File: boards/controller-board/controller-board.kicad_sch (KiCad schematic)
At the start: 163 parts, among them J1 Conn_01x02, J2 Conn_01x02, J3 Conn_01x02, J4 Conn_01x02, J5 Conn_01x03, J6 Conn_01x02, Q1 Goford_G11S_20V_11A, Q2 PMV45EN, SW1 EG1271, U1 CAT4201, U10 CAT4201, U11 CAT4201, U12 CAT4201, U13 CAT4201, U14 CAT4201, U15 CAT4201, U17 CAT4201, U18 CAT4201, U25 RPi_Pico, U3 LTC3624, U4 CAT4201, U5 CAT4201, U6 CAT4201, U7 MCP4728, U8 ADS1015IRUGR, U9 ADS1015IRUGR

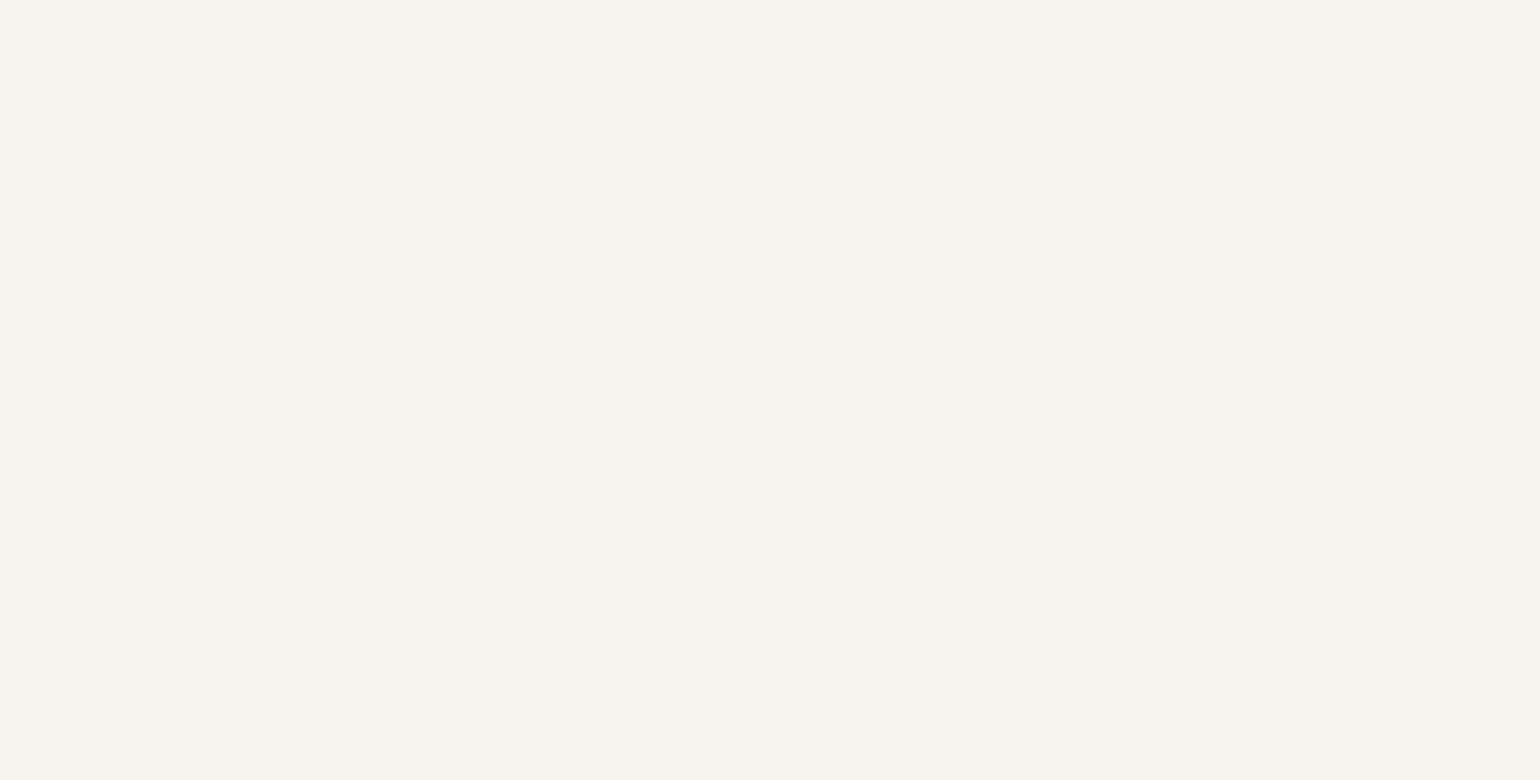
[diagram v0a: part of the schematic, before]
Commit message: added new design for LED driver portion of circuit with A6214
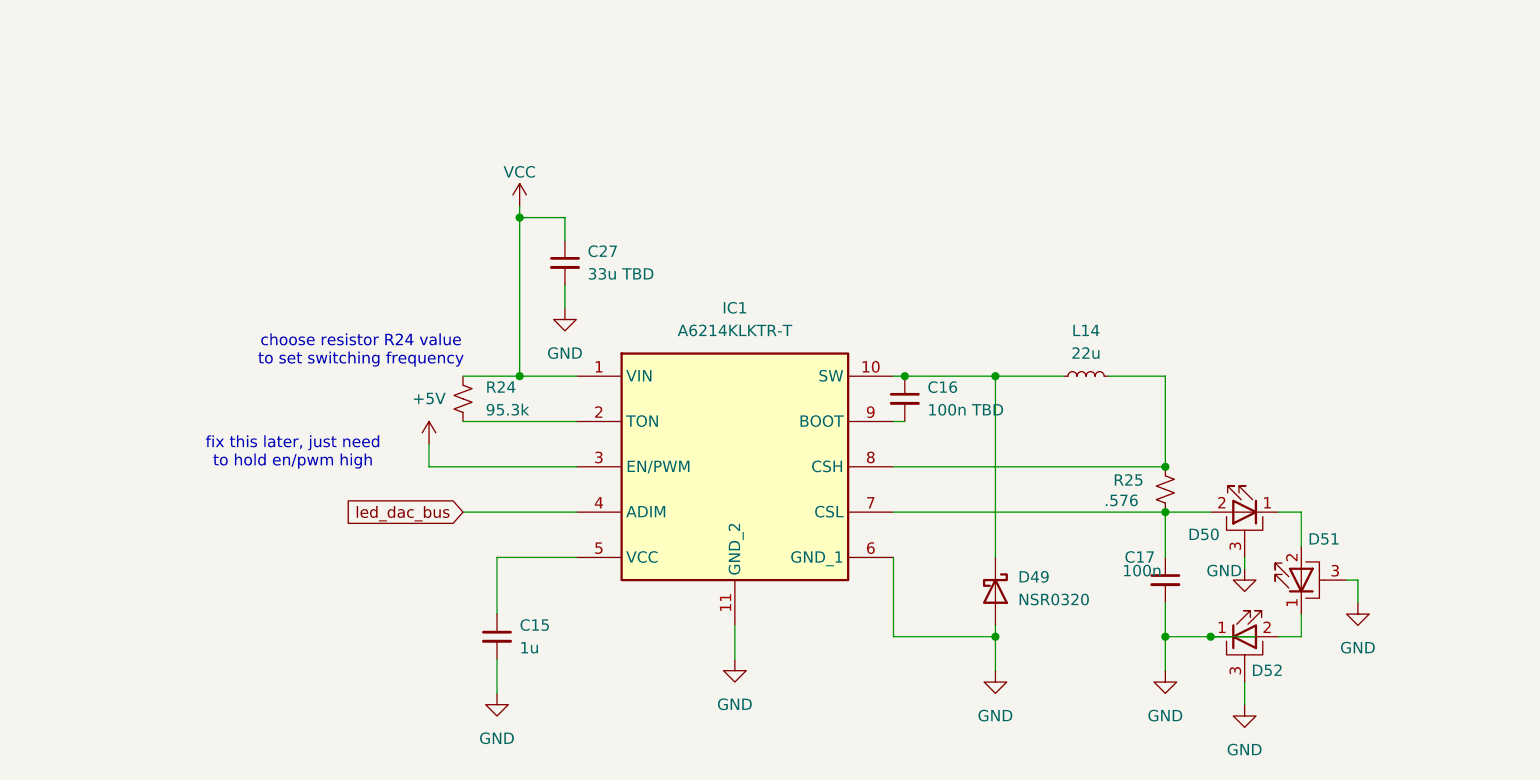
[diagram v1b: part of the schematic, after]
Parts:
- added C15: 1u, symbol Device:C_Small
- added C16: 100n TBD, symbol Device:C_Small
- added C17: 100n, symbol Device:C_Small
- added C27: 33u TBD, symbol Device:C_Small
- added D49: NSR0320, symbol Device:D_Schottky
- added D50, D51, D52: XPEBBL-L1-0000-00201, oresat-diodes:Cree-LED, symbol Device:LED_Pad
- added IC1: A6214KLKTR-T, oresat-ics:SOP100P600X165-11N, symbol oresat-ics:A6214KLKTR-T
- added L14: 22u, symbol Device:L_Small
- added R24: 95.3k, symbol Device:R_Small_US
- added R25: .576, symbol Device:R_Small_US
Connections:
- net +5V: now also IC1.3 (EN/PWM)
- net GND: now also C15.2, C17.2, C27.2, D49.2 (A), D50.3 (PAD), D51.3 (PAD), D52.1 (K), D52.3 (PAD), IC1.11 (GND_2), IC1.6 (GND_1)
- net VCC: now also C27.1, IC1.1 (VIN), R24.1
- new net: D51.1 (K), D52.2 (A)
- new net: C16.1, D49.1 (K), IC1.10 (SW), L14.1
- new net: IC1.2 (TON), R24.2
- new net: C15.1, IC1.5 (VCC)
- new net: C17.1, D50.2 (A), IC1.7 (CSL), R25.2
- new net: IC1.8 (CSH), L14.2, R25.1
- new net: C16.2, IC1.9 (BOOT)
- new net: D50.1 (K), D51.2 (A)
- new net led_dac_bus: IC1.4 (ADIM)
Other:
- note added: "choose resistor R24 value to set switching frequency"
- note added: "fix this later, just need to hold en/pwm high"

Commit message: added project for test board for new LED driver
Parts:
- removed C25, C34: 4.7u, Capacitor_SMD:C_0603_1608Metric, symbol Device:C_Small
- removed C26, C36: 22u, Capacitor_SMD:C_1210_3225Metric, symbol Device:C_Small
- removed D34, D7: NSR0320, Diode_SMD:D_SOD-323, symbol Device:D_Schottky
- removed D38, D39, D41: XPEBBL-L1-0000-00201, oresat-diodes:Cree-LED, symbol Device:LED_Pad
- removed D5, D6, D8: XPEBRD-L1-0000-00501, oresat-diodes:Cree-LED, symbol Device:LED_Pad
- removed L6, L9: 56u, Inductor_SMD:L_Wuerth_HCI-5040, symbol Device:L_Small
- removed R14, R18: 10k, Resistor_SMD:R_0603_1608Metric, symbol Device:R_Small_US
- removed U10, U13: CAT4201, Package_TO_SOT_SMD:TSOT-23-5, symbol oresat-ics:CAT4201
- added C32: 33u TBD, symbol Device:C_Small
- added C33: 1u, symbol Device:C_Small
- added C38: 100n TBD, symbol Device:C_Small
- added C39: 100n, symbol Device:C_Small
- added D53: NSR0320, symbol Device:D_Schottky
- added D54, D55, D56: XPEBBL-L1-0000-00201, oresat-diodes:Cree-LED, symbol Device:LED_Pad
- added IC2: A6214KLKTR-T, oresat-ics:SOP100P600X165-11N, symbol oresat-ics:A6214KLKTR-T
- added L15: 22u, symbol Device:L_Small
- added R26: 95.3k, symbol Device:R_Small_US
- added R27: .576, symbol Device:R_Small_US
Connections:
- net +5V: now also IC2.3 (EN/PWM)
- net GND: now also C32.2, C33.2, C39.2, D53.2 (A), D54.3 (PAD), D55.1 (K), D55.3 (PAD), D56.3 (PAD), IC2.11 (GND_2), IC2.6 (GND_1)
- net RED_LIM: no longer U1.1 (CTRL)
- net VCC: now also C32.1, IC2.1 (VIN), R26.1
- net led_dac_bus: now also IC2.4 (ADIM); no longer IC1.4 (ADIM)
- new net: IC2.8 (CSH), L15.2, R27.1
- new net: C39.1, D54.2 (A), IC2.7 (CSL), R27.2
- new net: D54.1 (K), D56.2 (A)
- new net: IC2.2 (TON), R26.2
- new net: C38.1, D53.1 (K), IC2.10 (SW), L15.1
- new net: C38.2, IC2.9 (BOOT)
- new net: D55.2 (A), D56.1 (K)
- new net: C33.1, IC2.5 (VCC)
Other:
- moved on the sheet: C1, C11, C12, C13, C16, C17, C2, C27, C28, C29, C3, C30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

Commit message: edited schematic to include new LED driver on new page
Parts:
- removed C1: 22u, oresat-diodes:Cree-LED, symbol Device:C_Small
- removed C11: 4.7u, Capacitor_SMD:C_0603_1608Metric, symbol Device:C_Small
- removed C32: 33u TBD, symbol Device:C_Small
- removed C33: 1u, symbol Device:C_Small
- removed C38: 100n TBD, symbol Device:C_Small
- removed C39: 100n, symbol Device:C_Small
- removed D1: NSR0320, Diode_SMD:D_SOD-323, symbol Device:D_Schottky
- removed D25, D26, D27: XPEBRD-L1-0000-00501, oresat-diodes:Cree-LED, symbol Device:LED_Pad
- removed D53: NSR0320, symbol Device:D_Schottky
- removed D54, D55, D56: XPEBBL-L1-0000-00201, oresat-diodes:Cree-LED, symbol Device:LED_Pad
- removed IC2: A6214KLKTR-T, oresat-ics:SOP100P600X165-11N, symbol oresat-ics:A6214KLKTR-T
- removed L1: 56u, Inductor_SMD:L_Wuerth_HCI-5040, symbol Device:L_Small
- removed L15: 22u, symbol Device:L_Small
- removed R2: 10k, Resistor_SMD:R_0603_1608Metric, symbol Device:R_Small_US
- removed R26: 95.3k, symbol Device:R_Small_US
- removed R27: .576, symbol Device:R_Small_US
- removed U1: CAT4201, Package_TO_SOT_SMD:TSOT-23-5, symbol oresat-ics:CAT4201
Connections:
- no-connect marks 26 -> 27
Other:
- added sheet Untitled Sheet (untitled.kicad_sch)
- note removed: "fix this later, just need to hold en/pwm high"

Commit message: cleaned up controller schematic
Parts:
- removed C15: 1u, symbol Device:C_Small
- removed C16: 100n TBD, symbol Device:C_Small
- removed C17: 100n, symbol Device:C_Small
- removed C27: 33u TBD, symbol Device:C_Small
- removed D49: NSR0320, symbol Device:D_Schottky
- removed D50, D51, D52: XPEBBL-L1-0000-00201, oresat-diodes:Cree-LED, symbol Device:LED_Pad
- removed IC1: A6214KLKTR-T, oresat-ics:SOP100P600X165-11N, symbol oresat-ics:A6214KLKTR-T
- removed L14: 22u, symbol Device:L_Small
- removed R24: 95.3k, symbol Device:R_Small_US
- removed R25: .576, symbol Device:R_Small_US
- renumbered C5 to C1, C9 to C10, C43 to C15, C44 to C16, C51 to C17, C20 to C18, C6 to C2, C2 to C20, C3 to C21, C28 to C22, C29 to C23, C12 to C24, C13 to C25, C30 to C26, C31 to C27, C35 to C28, C4 to C29, C10 to C3, C14 to C30, C45 to C31, C46 to C32, C37 to C33, C18 to C34, C40 to C35, C47 to C36, C48 to C37, C23 to C4, C21 to C5, C24 to C6, C22 to C7, C7 to C8, C8 to C9, D12 to D10, D9 to D11, D10 to D12, D30 to D13, D31 to D14, D28 to D15, D29 to D16, D14 to D17, D13 to D18, D33 to D19, D32 to D20, D35 to D21, D4 to D22, D17 to D23, D42 to D25, D36 to D26, D37 to D27, D20 to D28, D21 to D29, D18 to D30, D19 to D31, D45 to D32, D46 to D33, D43 to D34, D44 to D35, D40 to D36, D23 to D37, D22 to D38, D48 to D39, D47 to D40, D2 to D5, D3 to D6, D15 to D7, D16 to D8, D11 to D9, L5 to L1, L12 to L10, L13 to L11, L2 to L3, L3 to L4, L7 to L5, L8 to L6, L10 to L7, L4 to L8, L11 to L9, Q2 to Q1, Q1 to Q2, R15 to R10, R23 to R12, R10 to R13, R3 to R14, R4 to R15, R19 to R18, R5 to R19, R6 to R2, R7 to R3, R8 to R4, R9 to R5, R12 to R7, R13 to R8, R11 to R9, TP7 to TP1, TP6 to TP2, TP9 to TP3, TP1 to TP4, TP2 to TP5, TP3 to TP6, TP4 to TP7, TP5 to TP8, TP8 to TP9, U3 to U1, U14 to U10, U6 to U11, U15 to U12, U17 to U13, U18 to U14, U8 to U2, U9 to U3, U25 to U4, U7 to U5, U4 to U6, U5 to U7, U11 to U8, U12 to U9
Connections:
- no-connect marks 27 -> 26
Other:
- note removed: "choose resistor R24 value to set switching frequency"
- moved on the sheet: C1, C10, C15, C16, C17, C18, C19, C2, C20, C21, C22, C23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

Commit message: redesigned pcb
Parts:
- removed C20, C21, C22, C23, C28, C29, C30, C31, C32: 4.7u, Capacitor_SMD:C_0603_1608Metric, symbol Device:C_Small
- removed C24, C25, C26, C27, C33, C34, C35, C36, C37: 22u, Capacitor_SMD:C_1210_3225Metric, symbol Device:C_Small
- removed D10, D11, D12, D17, D18, D9: XPEBGR-L1-0000-00D01, oresat-diodes:Cree-LED, symbol Device:LED_Pad
- removed D13, D14, D15, D16, D19, D20, D26, D27, D36: XPEBBL-L1-0000-00201, oresat-diodes:Cree-LED, symbol Device:LED_Pad
- removed D21, D22, D23, D24, D25, D5, D6, D7, D8: NSR0320, Diode_SMD:D_SOD-323, symbol Device:D_Schottky
- removed D28, D29, D30, D31: ELUA3535OGB-P6070U23240500-VD1M, oresat-diodes:Cree-LED, symbol Device:LED_Pad
- removed D32, D33, D34, D35: ELUC3535NUB-P7085Q15070100-S22Q, oresat-diodes:Cree-LED, symbol Device:LED_Pad
- removed D37, D38, D39, D40: NP, oresat-diodes:Cree-LED, symbol Device:LED_Pad
- removed L10, L11, L3, L4, L5, L6, L7, L8, L9: 56u, Inductor_SMD:L_Wuerth_HCI-5040, symbol Device:L_Small
- removed R14, R15, R16, R17, R18, R19, R20, R21, R22: 10k, Resistor_SMD:R_0603_1608Metric, symbol Device:R_Small_US
- removed U10, U11, U12, U13, U14, U6, U7, U8, U9: CAT4201, Package_TO_SOT_SMD:TSOT-23-5, symbol oresat-ics:CAT4201
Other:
- note removed: "Blue LED Channel"
- note removed: "Green LED Channel"
- note removed: "Red LED Channel"
- note removed: "UV LED Channel"
- note removed: "double check PMV45EN symbol vs footprint - view datasheet pinout"
- moved on the sheet: C15, C16, C17, C18, C19, C4, C5, C6, C7, J2, J3, J4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

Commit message: added pull-down resistor to ADIM pins on LED drivers, completed BOM, reorganized schematic, switched 10k resistors and thermistors, added datasheets, split 12V pwr supply and added additional fuse, changed main pwr input connector to one with higher current rating
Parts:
- added F2: 10A, Fuse:Fuseholder_Littelfuse_Nano2_154x, symbol Device:Fuse_Small
- added F3: 0452008, symbol Device:Fuse_Small
- added F4: 0452005, Fuse:Fuseholder_Littelfuse_Nano2_154x, symbol Device:Fuse_Small
- added H1, H2, H3, H4, H5, H6, H7, H8, H9: MountingHole, oresat-misc:MountingHole_3.2mm_M3, symbol Mechanical:MountingHole
- C1, C15, C8, C9: DPN (none) -> 1276-CL32B226MOJVPNECT-ND; Distributor (none) -> DigiKey; MFR (none) -> Samsung Electro-Mechanics; MPN (none) -> CL32B226MOJVPNE
- C10, C19, C2, C6, C7: DPN (none) -> 490-6328-1-ND; Distributor (none) -> DigiKey; MFR (none) -> Murata Electronics; MPN (none) -> GRM155R71C104KA88J
- C16, C18, C4, C5: DPN (none) -> 311-1446-1-ND; Distributor (none) -> DigiKey; MFR (none) -> Yageo; MPN (none) -> CC0603KRX7R7BB105
- C17, J2, J3, J4, J5, TP1, TP10, TP11, TP12, TP13, TP2, TP3, TP4, TP5, TP6, TP7, TP8, TP9: Distributor (none) -> DigiKey
- C3: DPN (none) -> 445-6932-1-ND; Distributor (none) -> DigiKey; MFR (none) -> TDK Corporation; MPN (none) -> CGA3E1X5R1C225K080AC
- F1: DPN (none) -> 18-01550900DRCT-ND; Distributor (none) -> DigiKey; MFR (none) -> Littelfuse Inc.; MPN (none) -> 01550900DR
- J1: DPN (none) -> 277-1667-ND; Distributor (none) -> DigiKey; MFR (none) -> Phoenix Contact; MPN (none) -> 1935161
- J6: value Conn_01x02 -> Phoenix 1995499; DPN (none) -> 277-6718-ND; Distributor (none) -> DigiKey; MFR (none) -> Phoenix Contact; MPN (none) -> 1995499
- L1: DPN (none) -> XC2333CT-ND; Distributor (none) -> DigiKey; MFR (none) -> ECS Inc.; MPN (none) -> ECS-MPI4040R3-3R3-R
- Q1: DPN (none) -> 1727-2307-1-ND; Distributor (none) -> DigiKey; MFR (none) -> Nexperia USA Inc.; MPN (none) -> PMV45EN2R
- Q2: DPN (none) -> 3141-G11SCT-ND; Distributor (none) -> DigiKey; MFR (none) -> Goford Semiconductor; MPN (none) -> G11S
- R1, R2, R3, R9: DPN (none) -> 311-10.0KHRCT-ND; Distributor (none) -> DigiKey; MFR (none) -> Yageo; MPN (none) -> RC0603FR-0710KL
- R10, R4, R5: DPN (none) -> 311-100KHRCT-ND; Distributor (none) -> DigiKey; MFR (none) -> Yageo; MPN (none) -> RC0603FR-07100KL
- R12: DPN (none) -> 311-1.00KHRCT-ND; Distributor (none) -> DigiKey; MFR (none) -> Yageo; MPN (none) -> RC0603FR-071KL
- R13: DPN (none) -> 311-0.0GRCT-ND; Distributor (none) -> DigiKey; MFR (none) -> Yageo; MPN (none) -> RC0603JR-070RL
- R7, R8: DPN (none) -> 311-4.70KHRCT-ND; Distributor (none) -> DigiKey; MFR (none) -> Yageo; MPN (none) -> RC0603FR-074K7L
- SW1: DPN (none) -> EG1918-ND; Distributor (none) -> DigiKey; MFR (none) -> E-Switch; MPN (none) -> EG1271
- U1: DPN (none) -> LTC3624IDD-5#PBF-ND; Distributor (none) -> DigiKey; MFR (none) -> Analog Devices; MPN (none) -> LTC3624IDD-5#PBF
- U2, U3: DPN (none) -> 296-43557-1-ND; Distributor (none) -> DigiKey; MFR (none) -> Texas Instruments; MPN (none) -> ADS1015IRUGR
- U4: DPN (none) -> 2648-SC0917-ND; Distributor (none) -> DigiKey; MFR (none) -> Raspberry Pi; MPN (none) -> SC0917
- U5: DPN (none) -> MCP4728-E/UN-ND; MFR (none) -> Microchip Technology; MPN (none) -> MCP4728-E/UN
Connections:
- net +3.3V: now also R1.1, R2.1, R3.1; no longer J2.1 (Pin_1), J3.1 (Pin_1), J4.1 (Pin_1)
- net GND: now also J2.2 (Pin_2), J3.2 (Pin_2), J4.2 (Pin_2); no longer R1.2, R2.2, R3.2
- net SCL1: now also R7.2; no longer R8.2
- net SDA1: now also R8.2; no longer R7.2
- net THERM1: now also J2.1 (Pin_1), R1.2; no longer J2.2 (Pin_2), R1.1
- net THERM2: now also J3.1 (Pin_1), R2.2; no longer J3.2 (Pin_2), R2.1
- net THERM3: now also J4.1 (Pin_1), R3.2; no longer J4.2 (Pin_2), R3.1
- net at F1.1, J1.2 (Pin_2): now also TP1.1, F2.1
- net VCC renamed +12Vpwm
- net +12Vpwm: no longer TP1.1
- new net +12V: F2.2
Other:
- sheet Untitled Sheet renamed LED Drivers
- sheet LED Drivers: file untitled.kicad_sch -> led-drivers.kicad_sch
- note added: "Input from SS if stuffed"
- note added: "Need 12V/11A power supply"
- note added: "USB powered"
- note added: "should C15 and C1 have higher voltage ratings?"
- note added: "switch places for 10k and thermistor not photodiode though"
- note removed: "Input from SS"
- note removed: "OreSat Solar Simulator Controller Board v1.1"
- note removed: "switch places for 10k and thermistor"
- note removed: "switch to 4-layer board?"
- title: (none) -> OreSat Solar Simulator
- moved on the sheet: C1, C10, C15, C16, C17, C18, C19, C2, C3, C4, C5, C6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

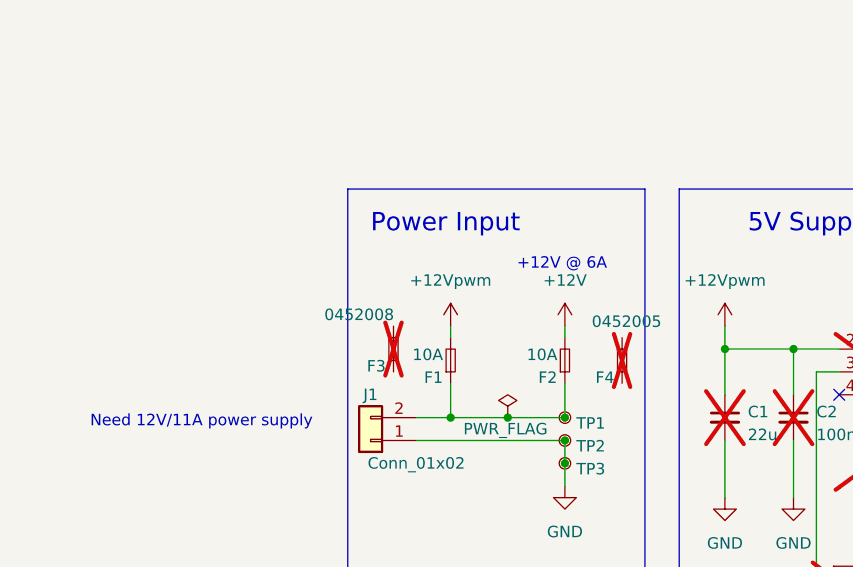
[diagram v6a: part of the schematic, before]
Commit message: minor changes to schematic, pcb, and BOM
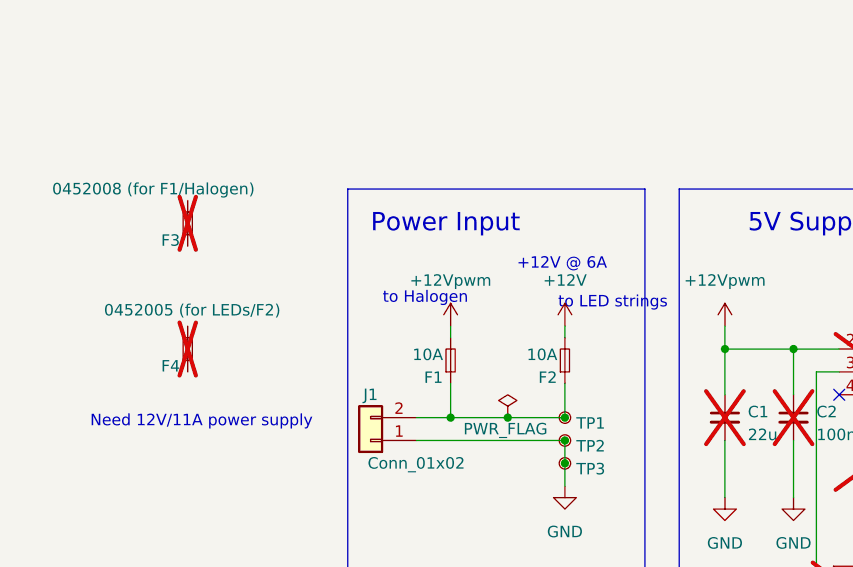
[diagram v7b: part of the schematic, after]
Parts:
- F3: value 0452008 -> 0452008 (for F1/Halogen)
- F4: value 0452005 -> 0452005 (for LEDs/F2)
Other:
- note added: "to Halogen"
- note added: "to LED strings"
- moved on the sheet: F3, F4
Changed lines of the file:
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@@
 		)
 	)
+	(text "to Halogen"
+		(exclude_from_sim no)
+		(at 158.496 57.912 0)
+		(effects
+			(font
+				(size 1.27 1.27)
+			)
+		)
+	)
 	(text "Output to SS"
 		(exclude_from_sim no)
@@
 		)
 	)
+	(text "to LED strings"
+		(exclude_from_sim no)
+		(at 179.324 58.42 0)
+		(effects
+			(font
+				(size 1.27 1.27)
+			)
+		)
+	)
 	(text "Power Input"
 		(exclude_from_sim no)
@@
 	(symbol
 		(lib_id "Device:Fuse_Small")
-		(at 180.34 64.77 90)
+		(at 132.08 63.5 90)
 		(unit 1)
 		(exclude_from_sim no)
@@
 		(dnp yes)
 		(property "Reference" "F4"
-			(at 178.435 66.675 90)
+			(at 130.175 65.405 90)
 			(effects
 				(font
@@
 			)
 		)
-		(property "Value" "0452005"
-			(at 180.848 60.452 90)
+		(property "Value" "0452005 (for LEDs/F2)"
+			(at 132.588 59.182 90)
 			(effects
 				(font
@@
 		)
 		(property "Footprint" "Fuse:Fuseholder_Littelfuse_Nano2_154x"
-			(at 180.34 64.77 0)
+			(at 132.08 63.5 0)
 			(effects
 				(font
@@
 		)
 		(property "Datasheet" "https://www.littelfuse.com/media?resourcetype=datasheets&itemid=8c87aa93-80a7-4ea8-8749-a19ba03901c2&filename=littelfuse-fuse-452-454-datasheet"
-			(at 180.34 64.77 0)
+			(at 132.08 63.5 0)
 			(effects
 				(font
@@
 		)
 		(property "Description" ""
-			(at 180.34 64.77 0)
+			(at 132.08 63.5 0)
 			(effects
 				(font
@@
 		)
 		(property "DPN" "F2607CT-ND"
-			(at 180.34 64.77 0)
+			(at 132.08 63.5 0)
 			(effects
 				(font
@@
 		)
 		(property "Distributor" "DigiKey"
-			(at 180.34 64.77 0)
+			(at 132.08 63.5 0)
 			(effects
 				(font
@@
 		)
 		(property "MFR" "Littelfuse Inc."
-			(at 180.34 64.77 0)
+			(at 132.08 63.5 0)
 			(effects
 				(font
@@
 		)
 		(property "MPN" "0452005.MRL"
-			(at 180.34 64.77 0)
+			(at 132.08 63.5 0)
 			(effects
 				(font
@@
 	(symbol
 		(lib_id "Device:Fuse_Small")
-		(at 154.94 63.5 90)
+		(at 132.08 49.53 90)
 		(unit 1)
 		(exclude_from_sim no)
@@
 		(dnp yes)
 		(property "Reference" "F3"
-			(at 153.035 65.405 90)
+			(at 130.175 51.435 90)
 			(effects
 				(font
@@
 			)
 		)
-		(property "Value" "0452008"
-			(at 151.13 59.69 90)
+		(property "Value" "0452008 (for F1/Halogen)"
+			(at 128.27 45.72 90)
 			(effects
 				(font
@@
 		)
 		(property "Footprint" ""
-			(at 154.94 63.5 0)
+			(at 132.08 49.53 0)
 			(effects
 				(font
@@
 		)
 		(property "Datasheet" "https://www.littelfuse.com/media?resourcetype=datasheets&itemid=8c87aa93-80a7-4ea8-8749-a19ba03901c2&filename=littelfuse-fuse-452-454-datasheet"
-			(at 154.94 63.5 0)
+			(at 132.08 49.53 0)
 			(effects
 				(font
@@
 		)
 		(property "Description" ""
-			(at 154.94 63.5 0)
+			(at 132.08 49.53 0)
 			(effects
 				(font
@@
 		)
 		(property "DPN" "F4172CT-ND"
-			(at 154.94 63.5 0)
+			(at 132.08 49.53 0)
 			(effects
 				(font
@@
 		)
 		(property "Distributor" "DigiKey"
-			(at 154.94 63.5 0)
+			(at 132.08 49.53 0)
 			(effects
 				(font
@@
 		)
 		(property "MFR" "Littelfuse Inc."
-			(at 154.94 63.5 0)
+			(at 132.08 49.53 0)
 			(effects
 				(font
@@
 		)
 		(property "MPN" "0452008.MRL"
-			(at 154.94 63.5 0)
+			(at 132.08 49.53 0)
 			(effects
 				(font
